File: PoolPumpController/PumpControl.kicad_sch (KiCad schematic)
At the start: 14 parts, among them J1 Screw_Terminal_01x02, J2 Screw_Terminal_01x02, Q1 2N7002, U3 MOC3021S

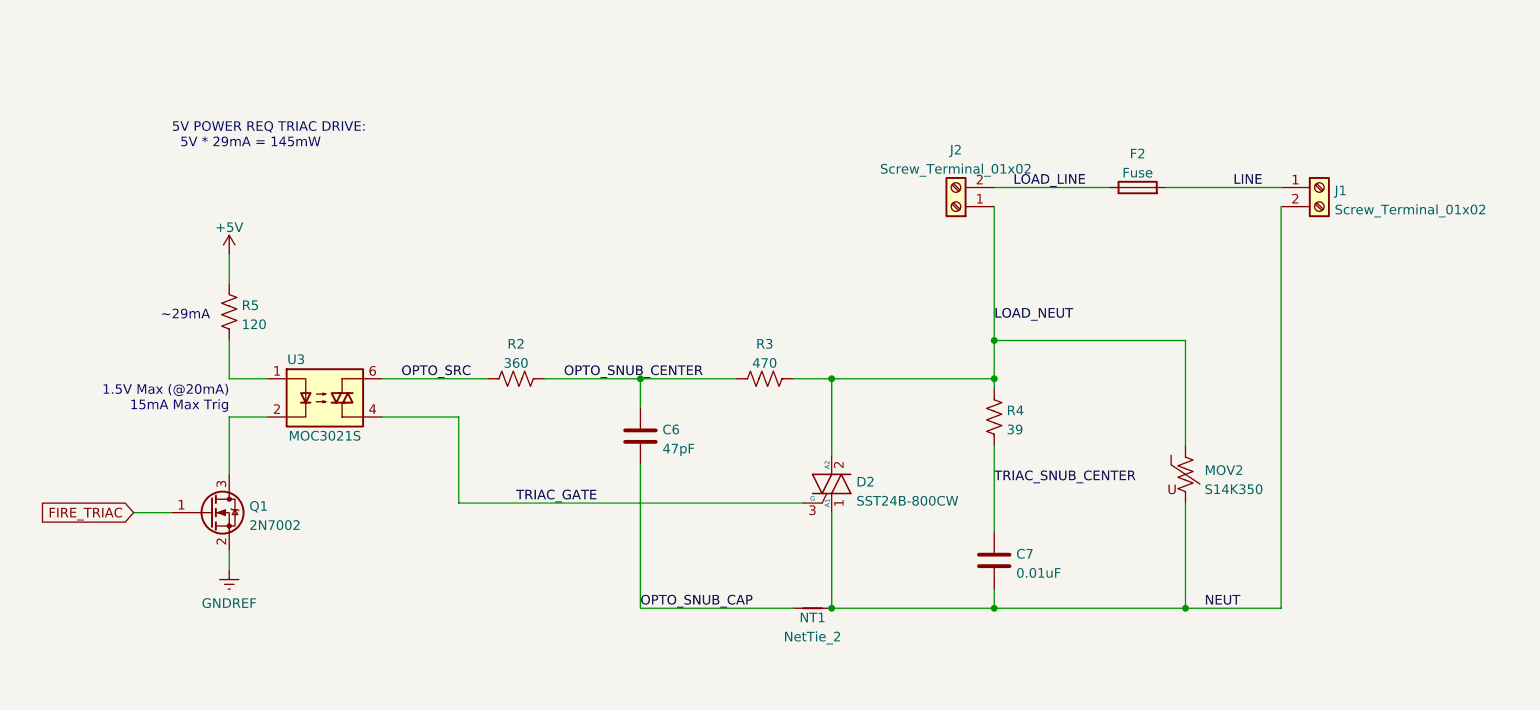
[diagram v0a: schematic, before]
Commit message: Changed screw terminal symbols used for power connections to test points that will be used for soldering wires from a panel mount connector.
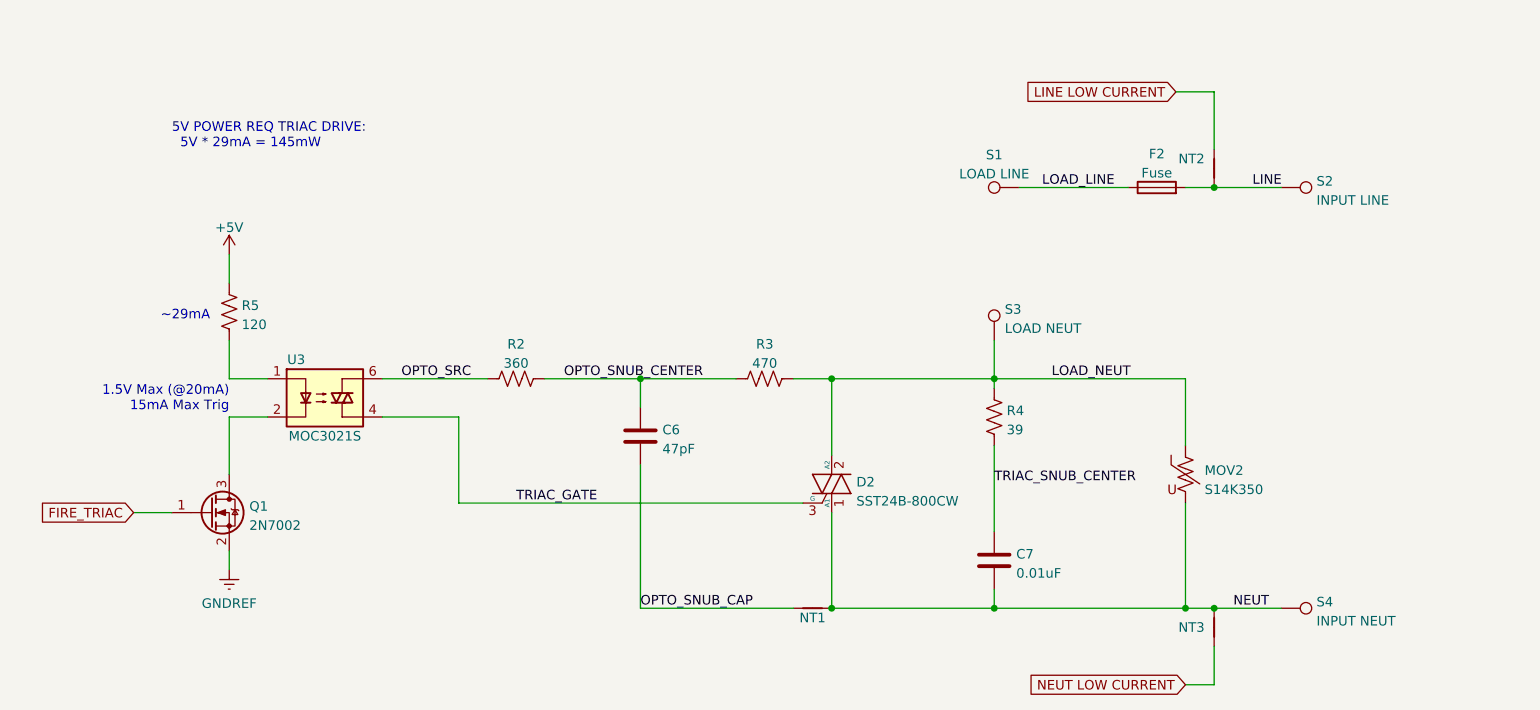
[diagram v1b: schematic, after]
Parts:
- removed J1, J2: Screw_Terminal_01x02, symbol Connector:Screw_Terminal_01x02
- added NT2, NT3: NetTie_2, symbol Device:NetTie_2
- added S1: LOAD LINE, symbol Connector:TestPoint
- added S2: INPUT LINE, symbol Connector:TestPoint
- added S3: LOAD NEUT, symbol Connector:TestPoint
- added S4: INPUT NEUT, symbol Connector:TestPoint
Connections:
- net LINE: now also NT2.1, S2.1
- net LOAD_LINE: now also S1.1
- net LOAD_NEUT: now also S3.1
- net NEUT: now also NT3.2, S4.1
- new net LINE LOW CURRENT: NT2.2
- new net NEUT LOW CURRENT: NT3.1
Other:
- moved on the sheet: F2

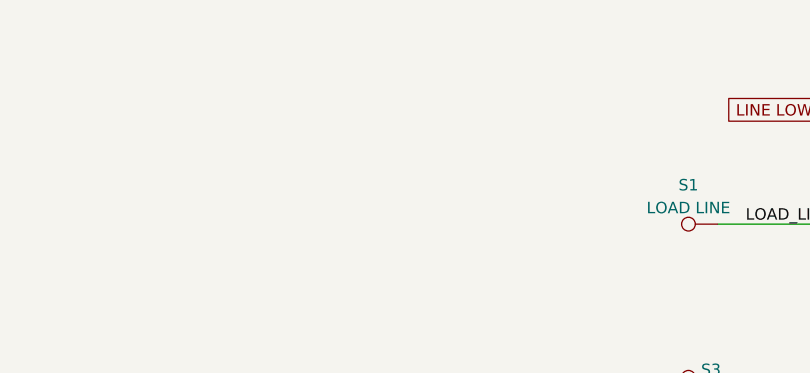
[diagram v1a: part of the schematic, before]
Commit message: Added Power Receptical for Pump Output
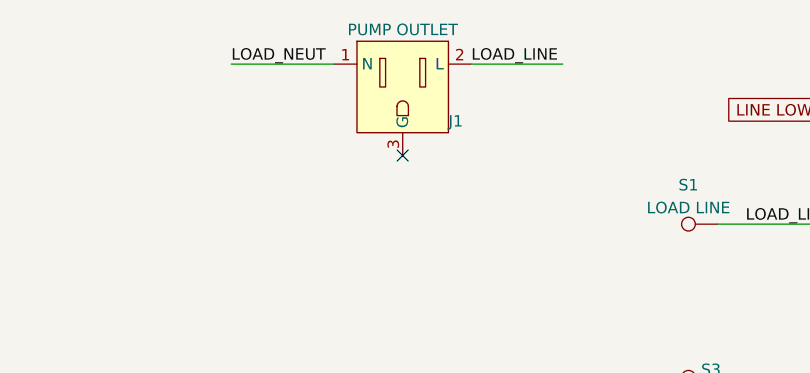
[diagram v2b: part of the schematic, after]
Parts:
- added J1: PUMP OUTLET, symbol JEDD-symbols:Power_Receptacle_120V
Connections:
- net LOAD_LINE: now also J1.2 (L)
- net LOAD_NEUT: now also J1.1 (N)
- no-connect marks 0 -> 1
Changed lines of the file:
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@@
   (junction (at 154.94 96.52) (diameter 0) (color 0 0 0 0)
   )
+  (no_connect (at 144.78 63.5))
   (wire (pts (xy 201.93 71.12) (xy 205.74 71.12))
     (stroke (width 0) (type default) (color 0 0 0 0))
@@
     (stroke (width 0) (type default) (color 0 0 0 0))
   )
+  (wire (pts (xy 152.4 53.34) (xy 162.56 53.34))
+    (stroke (width 0) (type default) (color 0 0 0 0))
+  )
   (wire (pts (xy 200.66 58.42) (xy 205.74 58.42))
     (stroke (width 0) (type default) (color 0 0 0 0))
@@
   )
   (wire (pts (xy 80.01 101.6) (xy 74.93 101.6))
+    (stroke (width 0) (type default) (color 0 0 0 0))
+  )
+  (wire (pts (xy 125.73 53.34) (xy 137.16 53.34))
     (stroke (width 0) (type default) (color 0 0 0 0))
   )
@@
   )
   (label "LINE" (at 210.82 71.12 0)
+    (effects (font (size 1.27 1.27)) (justify left bottom))
+  )
+  (label "LOAD_LINE" (at 152.4 53.34 0)
+    (effects (font (size 1.27 1.27)) (justify left bottom))
+  )
+  (label "LOAD_NEUT" (at 125.73 53.34 0)
     (effects (font (size 1.27 1.27)) (justify left bottom))
   )
@@
     (pin "1")
   )
+  (symbol (lib_id "JEDD-symbols:Power_Receptacle_120V") (at 144.78 55.88 0) (unit 1)
+    (in_bom yes) (on_board no)
+    (property "Reference" "J1" (id 0) (at 149.86 59.69 0)
+      (effects (font (size 1.27 1.27)) (justify left))
+    )
+    (property "Value" "PUMP OUTLET" (id 1) (at 144.78 49.53 0))
+    (property "Footprint" "" (id 2) (at 144.78 55.88 0)
+      (effects (font (size 1.27 1.27)) hide)
+    )
+    (property "Datasheet" "https://us.schurter.com/en/datasheet/typ_NR020.pdf" (id 3) (at 144.78 55.88 0)
+      (effects (font (size 1.27 1.27)) hide)
+    )
+    (property "Digikey PN" "486-3-119-051-ND" (id 4) (at 144.78 55.88 0)
+      (effects (font (size 1.27 1.27)) hide)
+    )
+    (pin "1")
+    (pin "2")
+    (pin "3")
+  )
   (symbol (lib_id "Device:Q_TRIAC_A1A2G") (at 154.94 110.49 0) (unit 1)

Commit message: Added footprints to power IO. Updated gitignore to ignore LTSpice simulation raw and log files.
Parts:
- NT1, NT2, NT3: footprint (none) -> NetTie:NetTie-2_SMD_Pad0.5mm
- S1, S2, S3, S4: footprint (none) -> TestPoint:TestPoint_Plated_Hole_D3.0mm
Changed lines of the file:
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@@
       (effects (font (size 1.27 1.27)) (justify left))
     )
-    (property "Footprint" "" (id 2) (at 214.63 132.08 0)
+    (property "Footprint" "TestPoint:TestPoint_Plated_Hole_D3.0mm" (id 2) (at 214.63 132.08 0)
       (effects (font (size 1.27 1.27)) hide)
     )
@@
       (effects (font (size 1.27 1.27)) hide)
     )
-    (property "Footprint" "" (id 2) (at 205.74 68.58 0)
+    (property "Footprint" "NetTie:NetTie-2_SMD_Pad0.5mm" (id 2) (at 205.74 68.58 0)
       (effects (font (size 1.27 1.27)) hide)
     )
@@
       (effects (font (size 1.27 1.27)) (justify left))
     )
-    (property "Footprint" "" (id 2) (at 181.61 91.44 0)
+    (property "Footprint" "TestPoint:TestPoint_Plated_Hole_D3.0mm" (id 2) (at 181.61 91.44 0)
       (effects (font (size 1.27 1.27)) hide)
     )
@@
       (effects (font (size 1.27 1.27)) hide)
     )
-    (property "Footprint" "" (id 2) (at 205.74 129.54 0)
+    (property "Footprint" "NetTie:NetTie-2_SMD_Pad0.5mm" (id 2) (at 205.74 129.54 0)
       (effects (font (size 1.27 1.27)) hide)
     )
@@
     (property "Reference" "S1" (id 0) (at 176.53 66.7852 90))
     (property "Value" "LOAD LINE" (id 1) (at 176.53 69.3221 90))
-    (property "Footprint" "" (id 2) (at 179.832 66.04 0)
+    (property "Footprint" "TestPoint:TestPoint_Plated_Hole_D3.0mm" (id 2) (at 179.832 66.04 0)
       (effects (font (size 1.27 1.27)) hide)
     )
@@
       (effects (font (size 1.27 1.27)) (justify left))
     )
-    (property "Footprint" "" (id 2) (at 214.63 76.2 0)
+    (property "Footprint" "TestPoint:TestPoint_Plated_Hole_D3.0mm" (id 2) (at 214.63 76.2 0)
       (effects (font (size 1.27 1.27)) hide)
     )
@@
       (effects (font (size 1.27 1.27)) hide)
     )
-    (property "Footprint" "" (id 2) (at 152.4 127 0)
-      (effects (font (size 1.27 1.27)) hide)
-    )
+    (property "Footprint" "NetTie:NetTie-2_SMD_Pad0.5mm" (id 2) (at 152.4 127 0)
+      (effects (font (size 1.27 1.27)) hide)
+    )
